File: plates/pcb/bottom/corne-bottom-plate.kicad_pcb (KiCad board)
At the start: 2 copper layers, 133.8 x 91.4 mm, 7 parts

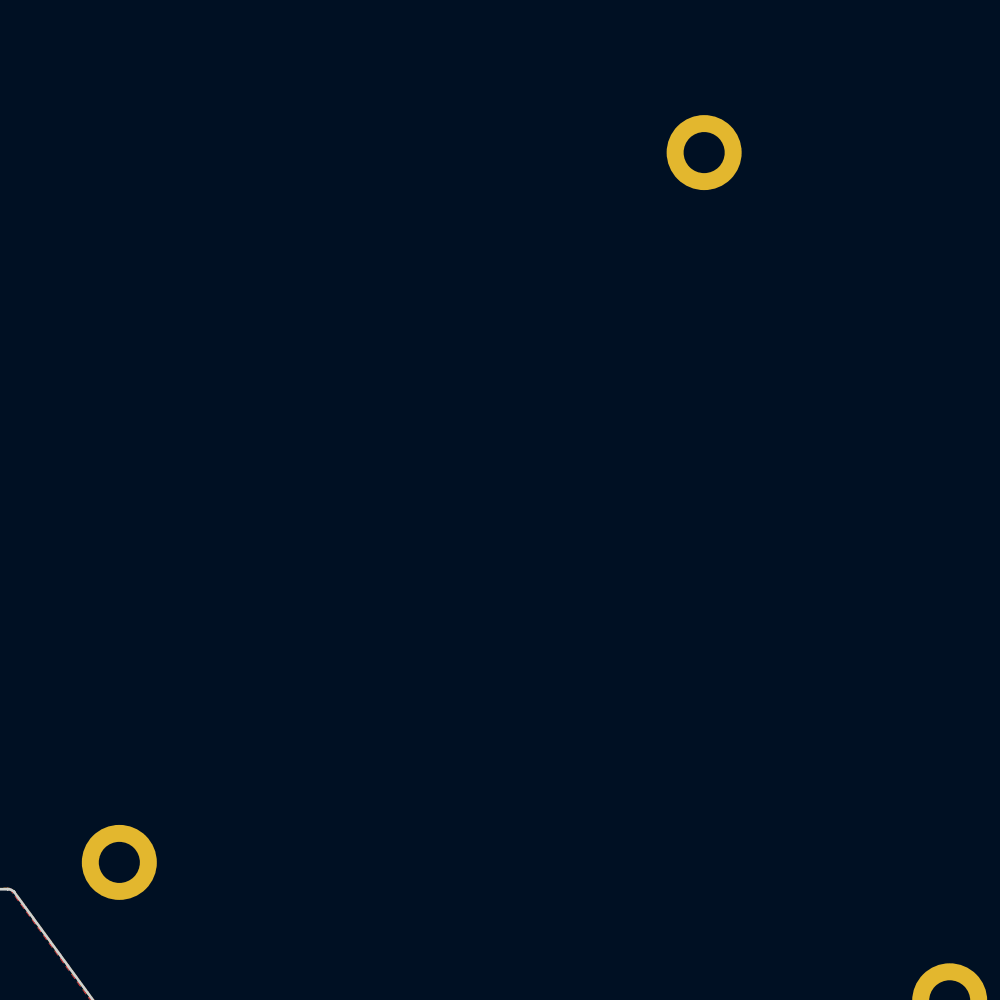
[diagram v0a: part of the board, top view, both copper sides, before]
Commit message: added support for tenting puck in bottom plate
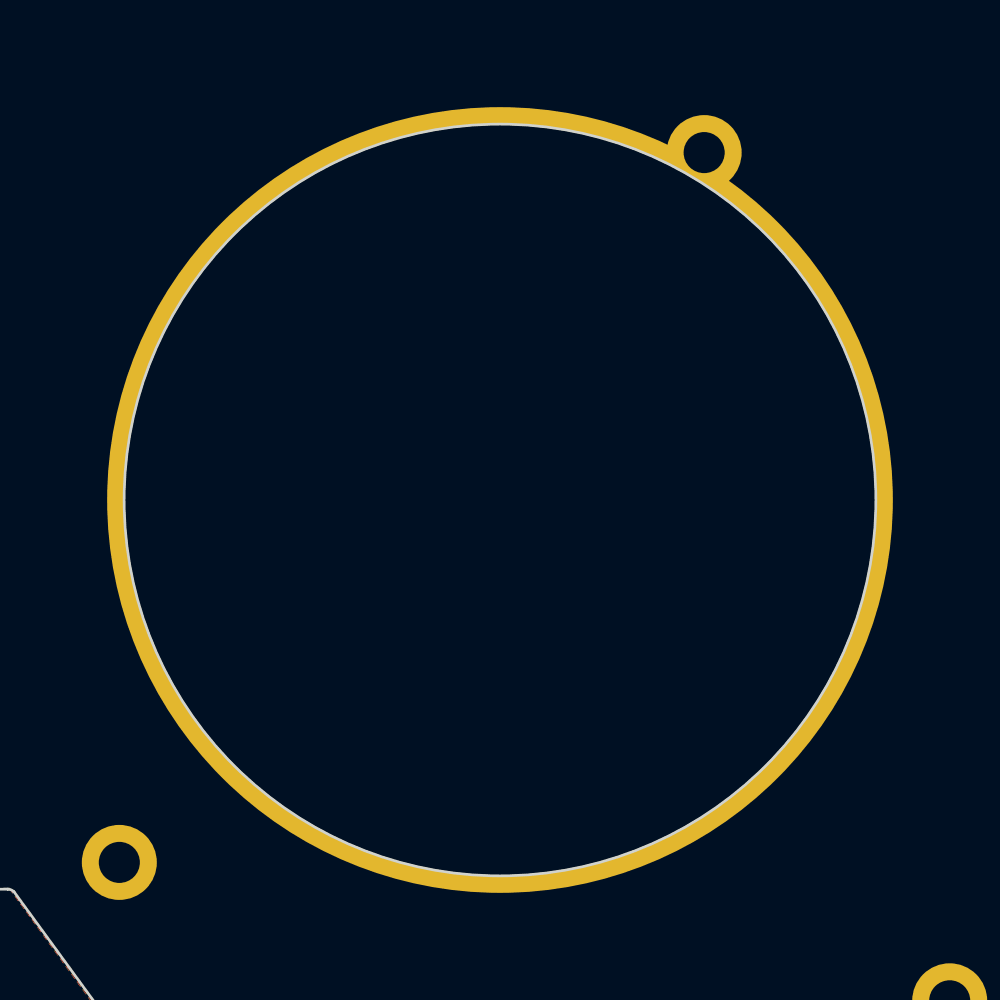
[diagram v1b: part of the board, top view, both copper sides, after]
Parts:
- removed G*** (x2): LOGO, kbd:corne-horizontal
- added ?: , kbd:M2_Hole_TH, F.Cu at (144.1, 102.5)
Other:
- outline, holes or cut-outs redrawn

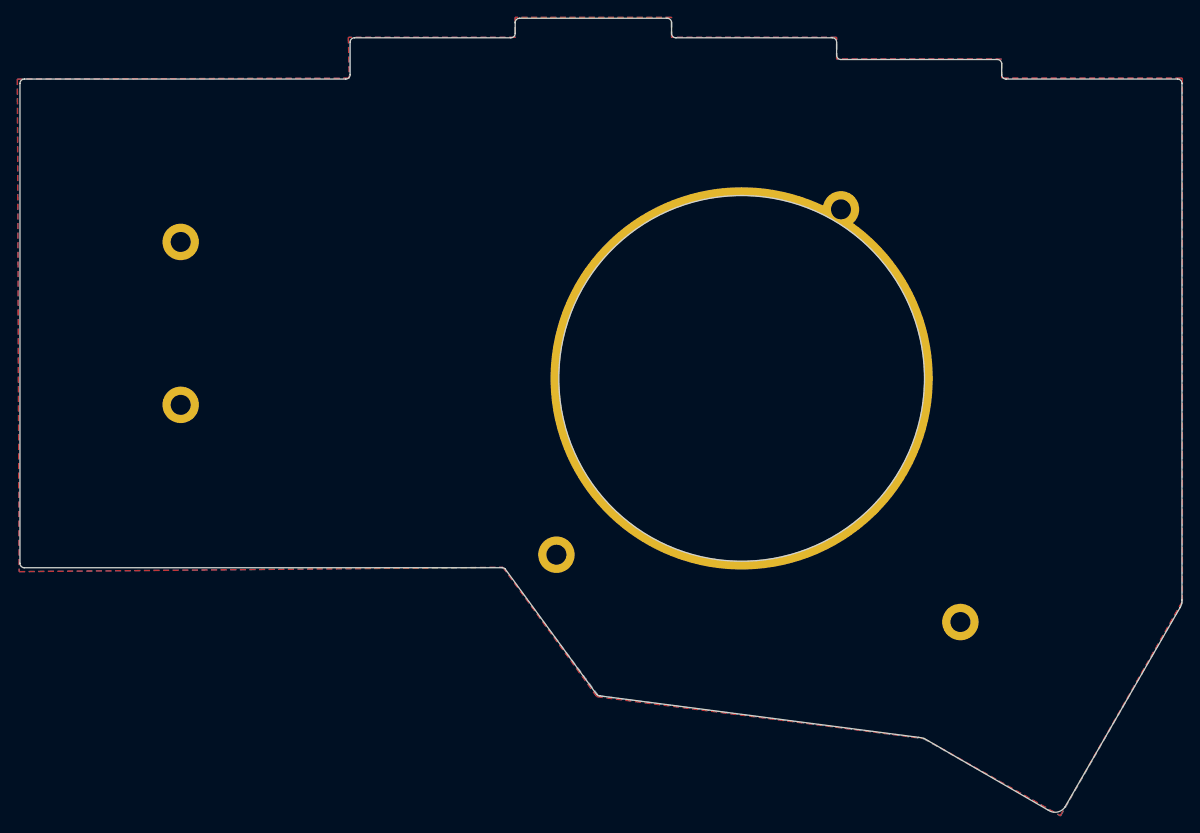
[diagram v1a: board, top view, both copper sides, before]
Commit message: adjusted position of tenting puck to match switch cut outs in top plate of case
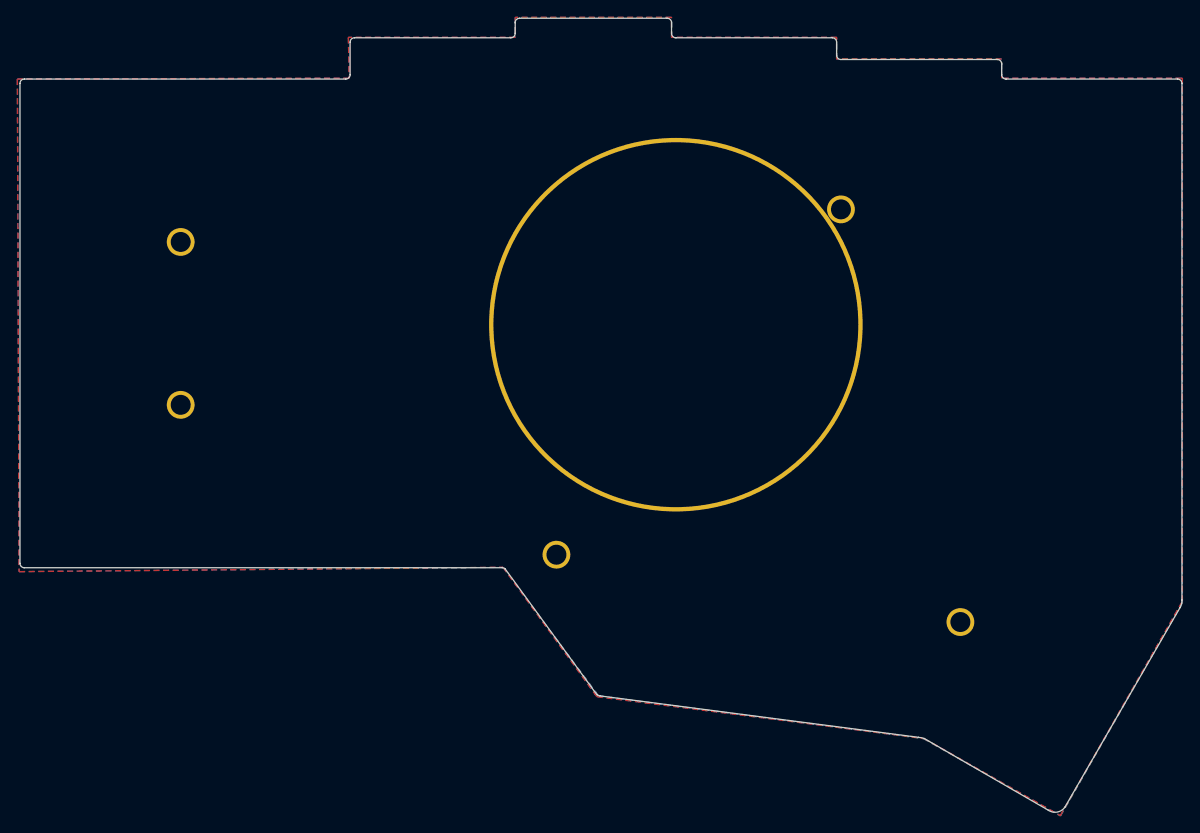
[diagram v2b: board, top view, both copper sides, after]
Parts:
- moved ? 9.77 mm to (136.5, 96.3)
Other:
- outline, holes or cut-outs redrawn
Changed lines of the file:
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@@
   (general
     (thickness 1.6)
-    (drawings 52)
+    (drawings 51)
     (tracks 0)
     (zones 0)
@@
   )
   (layers
-    (0 F.Cu signal hide)
-    (31 B.Cu signal hide)
+    (0 F.Cu signal)
+    (31 B.Cu signal)
     (32 B.Adhes user hide)
     (33 F.Adhes user hide)
     (34 B.Paste user hide)
     (35 F.Paste user hide)
-    (36 B.SilkS user hide)
-    (37 F.SilkS user hide)
+    (36 B.SilkS user)
+    (37 F.SilkS user)
     (38 B.Mask user)
     (39 F.Mask user)
@@
     (43 Eco2.User user hide)
     (44 Edge.Cuts user)
-    (45 Margin user)
-    (46 B.CrtYd user)
-    (47 F.CrtYd user)
-    (48 B.Fab user)
-    (49 F.Fab user)
+    (45 Margin user hide)
+    (46 B.CrtYd user hide)
+    (47 F.CrtYd user hide)
+    (48 B.Fab user hide)
+    (49 F.Fab user hide)
   )
   (setup
@@
     (mod_text_size 1 1)
     (mod_text_width 0.15)
-    (pad_size 4 4)
-    (pad_drill 2.2)
+    (pad_size 3.2 3.2)
+    (pad_drill 2.3)
     (pad_to_mask_clearance 0)
     (aux_axis_origin 194.75 68)
@@
   )
   (module kbd:M2_Hole_TH (layer F.Cu)
-    (at 144.0673 102.45492)
+    (at 136.4973 96.27492)
     (fp_text reference "" (at 0 -3.2) (layer F.SilkS)
       (effects (font (size 1 1) (thickness 0.15)))
@@
       (effects (font (size 1 1) (thickness 0.15)))
     )
-    (pad "" thru_hole circle (at 0 0) (size 44 44) (drill 42) (layers *.Cu *.Mask))
+    (pad "" thru_hole circle (at 0 0) (size 43 43) (drill 42) (layers *.Cu *.Mask))
   )
   (module kbd:M2_Hole_TH (layer F.Cu)
@@
       (effects (font (size 1 1) (thickness 0.15)))
     )
-    (pad "" thru_hole circle (at 0 0) (size 4.2 4.2) (drill 2.3) (layers *.Cu *.Mask))
+    (pad "" thru_hole circle (at 0 0) (size 3.2 3.2) (drill 2.3) (layers *.Cu *.Mask))
   )
   (module kbd:M2_Hole_TH (layer F.Cu)
@@
       (effects (font (size 1 1) (thickness 0.15)))
     )
-    (pad "" thru_hole circle (at 0 0) (size 4.2 4.2) (drill 2.3) (layers *.Cu *.Mask))
+    (pad "" thru_hole circle (at 0 0) (size 3.2 3.2) (drill 2.3) (layers *.Cu *.Mask))
   )
   (module kbd:M2_Hole_TH (layer F.Cu)
@@
       (effects (font (size 1 1) (thickness 0.15)))
     )
-    (pad "" thru_hole circle (at 0 0) (size 4.2 4.2) (drill 2.3) (layers *.Cu *.Mask))
+    (pad "" thru_hole circle (at 0 0) (size 3.2 3.2) (drill 2.3) (layers *.Cu *.Mask))
   )
   (module kbd:M2_Hole_TH (layer F.Cu)
@@
       (effects (font (size 1 1) (thickness 0.15)))
     )
-    (pad "" thru_hole circle (at 0 0) (size 4.2 4.2) (drill 2.3) (layers *.Cu *.Mask))
+    (pad "" thru_hole circle (at 0 0) (size 3.2 3.2) (drill 2.3) (layers *.Cu *.Mask))
   )
   (module kbd:M2_Hole_TH (layer F.Cu)
@@
       (effects (font (size 1 1) (thickness 0.15)))
     )
-    (pad "" thru_hole circle (at 0 0) (size 4.2 4.2) (drill 2.3) (layers *.Cu *.Mask))
+    (pad "" thru_hole circle (at 0 0) (size 3.2 3.2) (drill 2.3) (layers *.Cu *.Mask))
   )
-  (gr_circle (center 144.0673 102.45492) (end 123.25962 99.28246) (layer Edge.Cuts) (width 0.15))
   (gr_line (start 169.25 128.05) (end 169.25 132.950063) (layer F.Fab) (width 0.1))
   (gr_line (start 166.8 130.5) (end 171.7 130.5) (layer F.Fab) (width 0.1))
